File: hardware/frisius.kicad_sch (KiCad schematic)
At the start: 0 parts

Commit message: train schematics
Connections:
- no-connect marks 0 -> 2
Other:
- added sheet Mechanical (mech.kicad_sch)
- sheet GPS ports: added SENSOR_I2C{SDA SCL}; removed none
- sheet Processor ports: added BTN{BOOT NAV_A PWR RST}; removed BTN{BOOT NAV PWR RST}
- sheet Sensors ports: added IMU_INT1, IMU_INT2; removed none
- company: Erdapfel -> Frisius

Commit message: usb, charger, sensors, heir
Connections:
- no-connect marks 2 -> 0

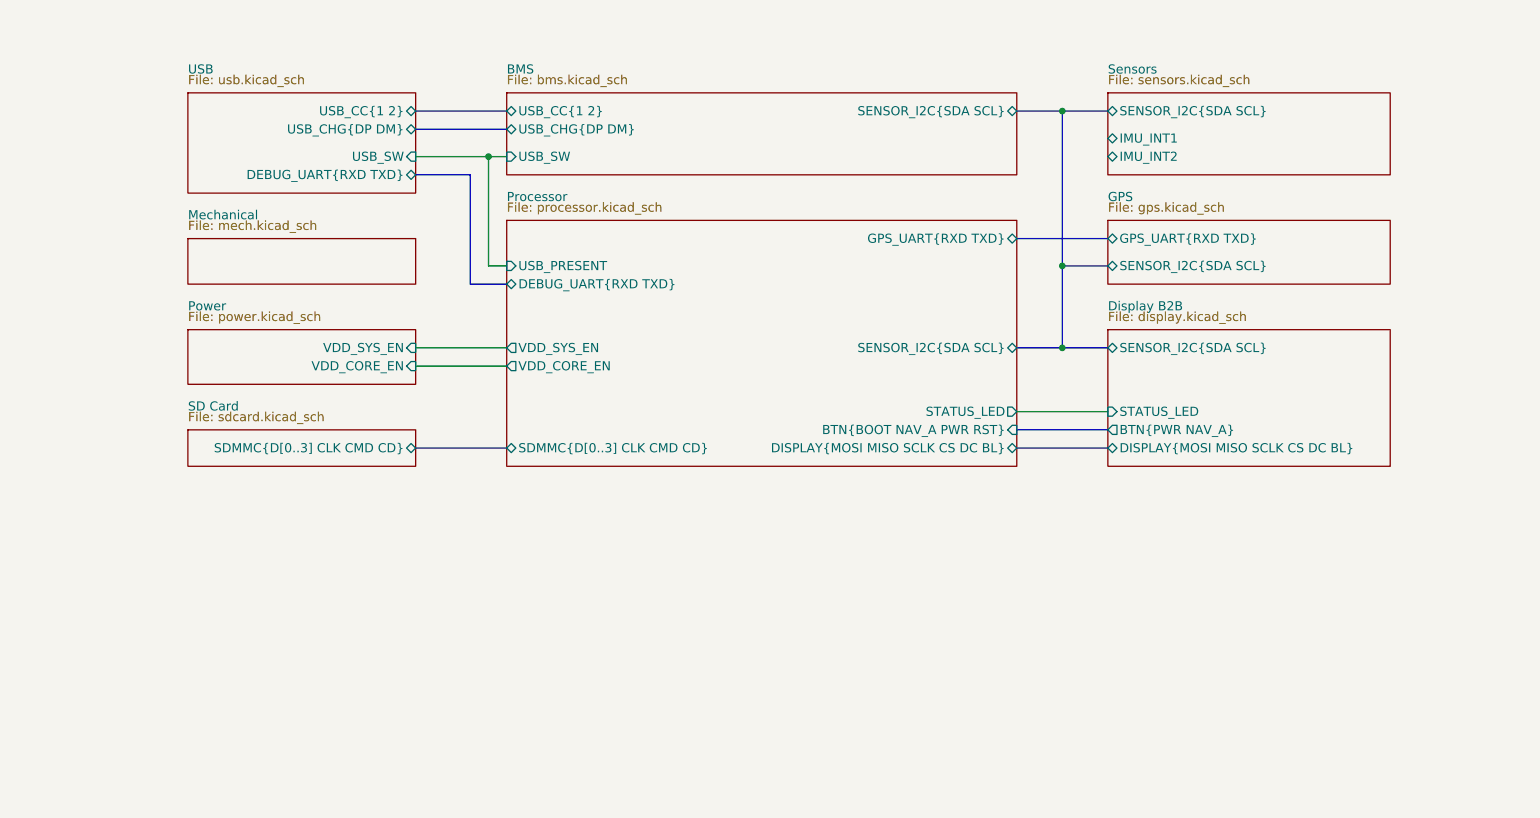
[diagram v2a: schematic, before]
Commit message: usb, bms, proc, btn changes
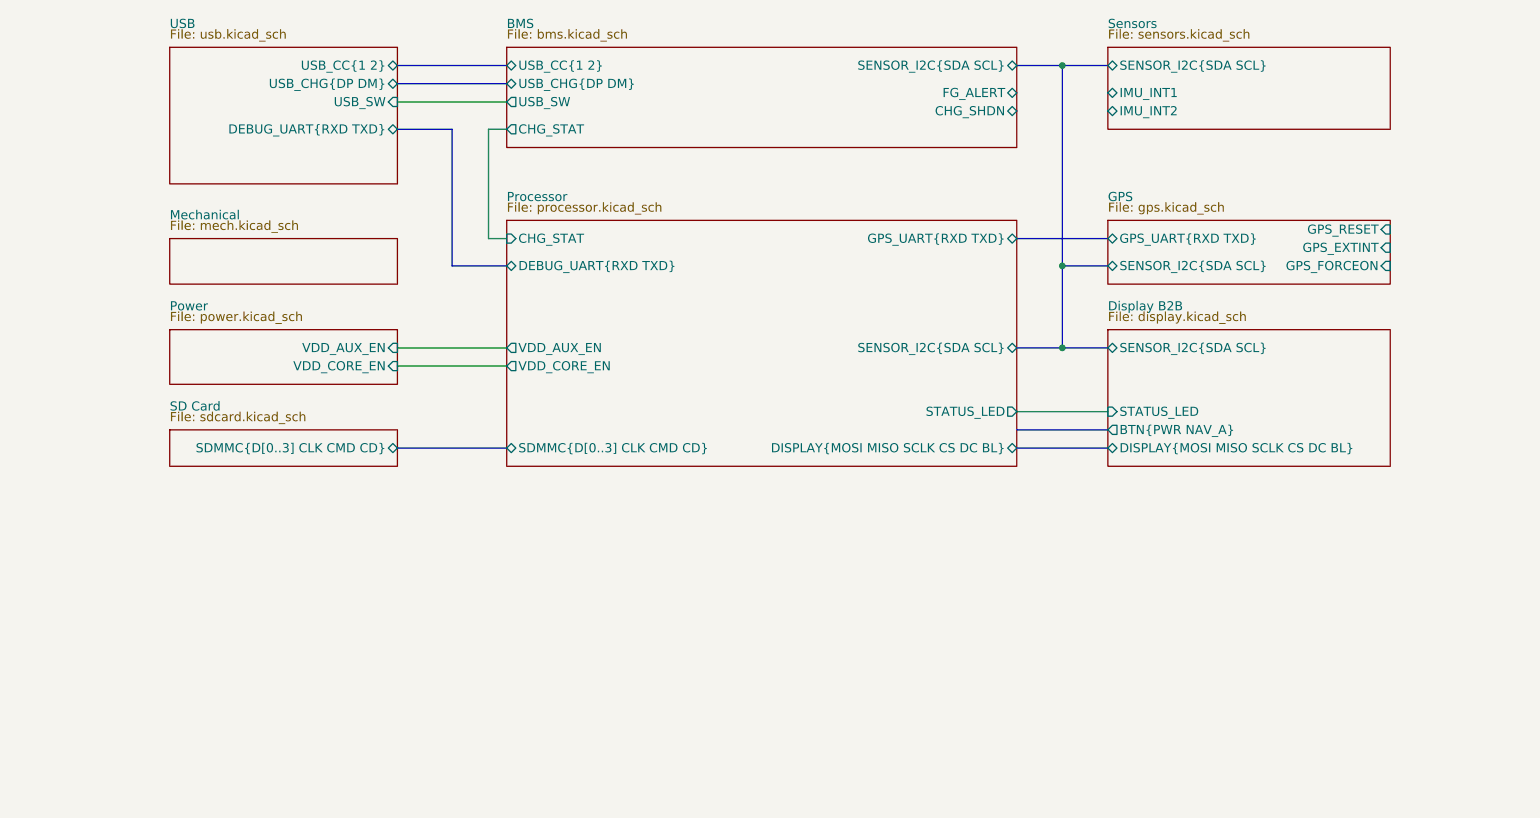
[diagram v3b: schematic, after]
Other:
- sheet BMS ports: added CHG_SHDN, CHG_STAT, FG_ALERT; removed none
- sheet GPS ports: added GPS_EXTINT, GPS_FORCEON, GPS_RESET; removed none
- sheet Power ports: added VDD_AUX_EN; removed VDD_SYS_EN
- sheet Processor ports: added CHG_STAT, VDD_AUX_EN; removed BTN{BOOT NAV_A PWR RST}, USB_PRESENT, VDD_SYS_EN

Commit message: started b2b and power
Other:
- sheet BMS ports: added CHARGE_SHDN, CHARGE_STAT, POWER_GOOD; removed CHG_SHDN, CHG_STAT, FG_ALERT, USB_SW
- sheet Display B2B ports: added VDD_AUX_EN; removed none
- sheet GPS ports: added none; removed GPS_EXTINT, GPS_FORCEON, GPS_RESET
- sheet Processor ports: added CHARGE_STAT, DEV_BTN{BOOT RST}, USB_PRESENT, USR_BTN{NAV_A PWR}; removed CHG_STAT
- sheet Sensors ports: added none; removed IMU_INT2
- sheet USB ports: added DEV_BTN{BOOT RST}; removed none

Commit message: ready for first review
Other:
- sheet Power ports: added CORE_BOOTSTRAP; removed none

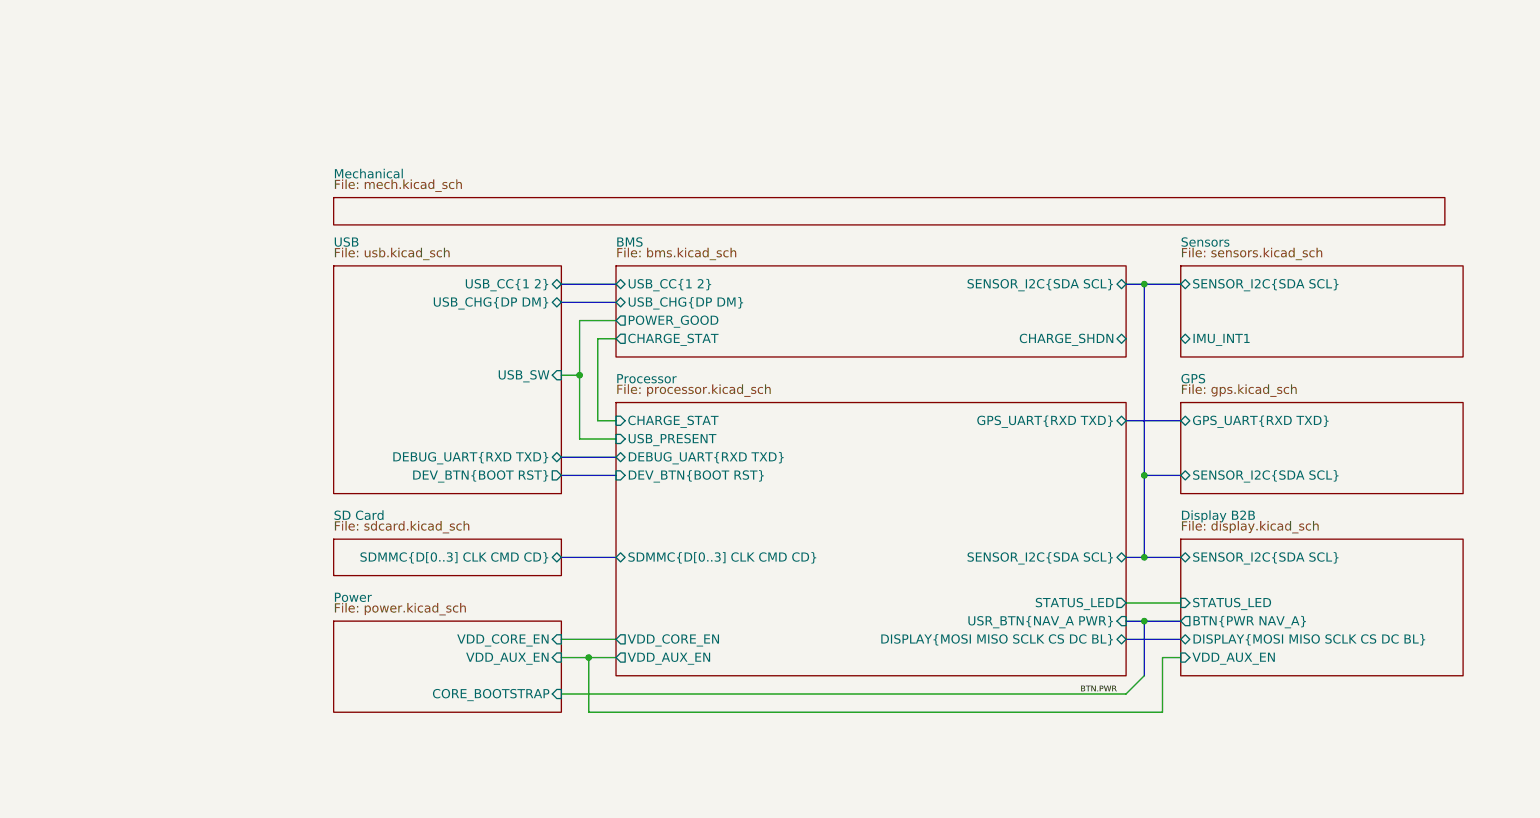
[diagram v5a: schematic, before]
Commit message: checking footprint assignment, added current sense pac1934 for dev
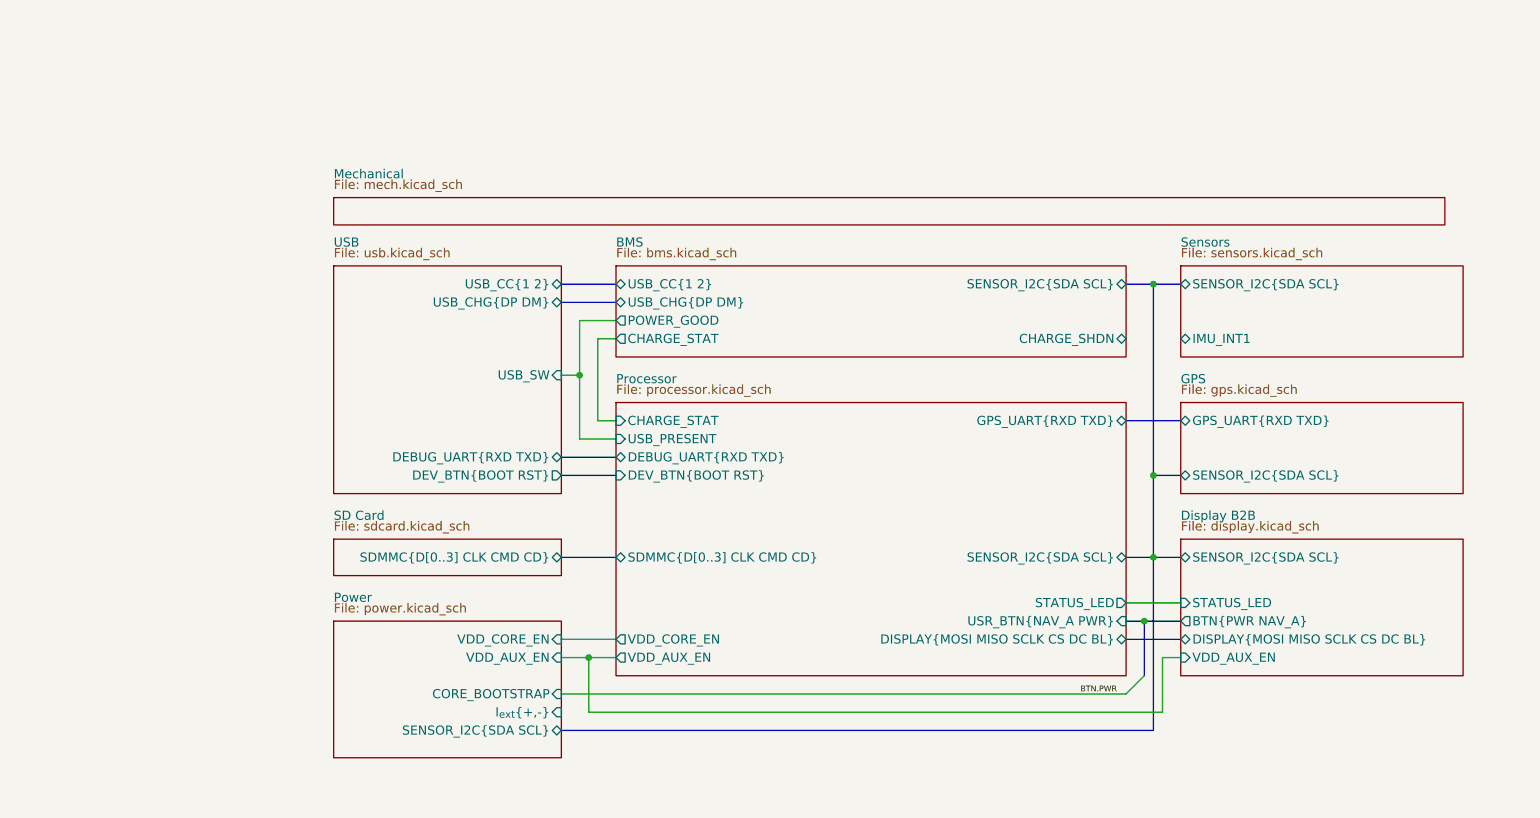
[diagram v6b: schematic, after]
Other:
- sheet Power ports: added I_{ext}{+,-}, SENSOR_I2C{SDA SCL}; removed none

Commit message: hardware update
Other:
- sheet BMS ports: added I_{bat}{+,-}, USB_CHG{D+ D-}; removed CHARGE_SHDN, CHARGE_STAT, USB_CHG{DP DM}
- sheet Display B2B ports: added USR_BTN{NAV_A PWR}; removed BTN{PWR NAV_A}
- sheet Power ports: added BOOTSTRAP, I_{bat}{+,-}, PWR_CTRL{CORE_EN AUX_EN}; removed CORE_BOOTSTRAP, I_{ext}{+,-}, VDD_AUX_EN, VDD_CORE_EN
- sheet Processor ports: added PCTRL{CORE_EN AUX_EN}; removed CHARGE_STAT, VDD_AUX_EN, VDD_CORE_EN
- sheet Sensors ports: added none; removed IMU_INT1
- sheet USB ports: added USB_CHG{D+ D-}; removed USB_CHG{DP DM}

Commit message: initial component placement and design simplification
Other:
- sheet GPS ports: added GPS_UART{RX TX}; removed GPS_UART{RXD TXD}
- sheet Processor ports: added GPS_UART{RX TX}; removed GPS_UART{RXD TXD}
